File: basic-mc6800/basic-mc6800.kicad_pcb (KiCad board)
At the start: 2 copper layers, 100 x 45 mm, 21 parts, among them J1 Conn_01x39_Male, Q1 Q_NMOS_GSD, Q2 Q_NMOS_GSD, U1 74LS137, U2 MC6809, U3 IS61C256AL, U4 28C256, Y1 2-4Mhz

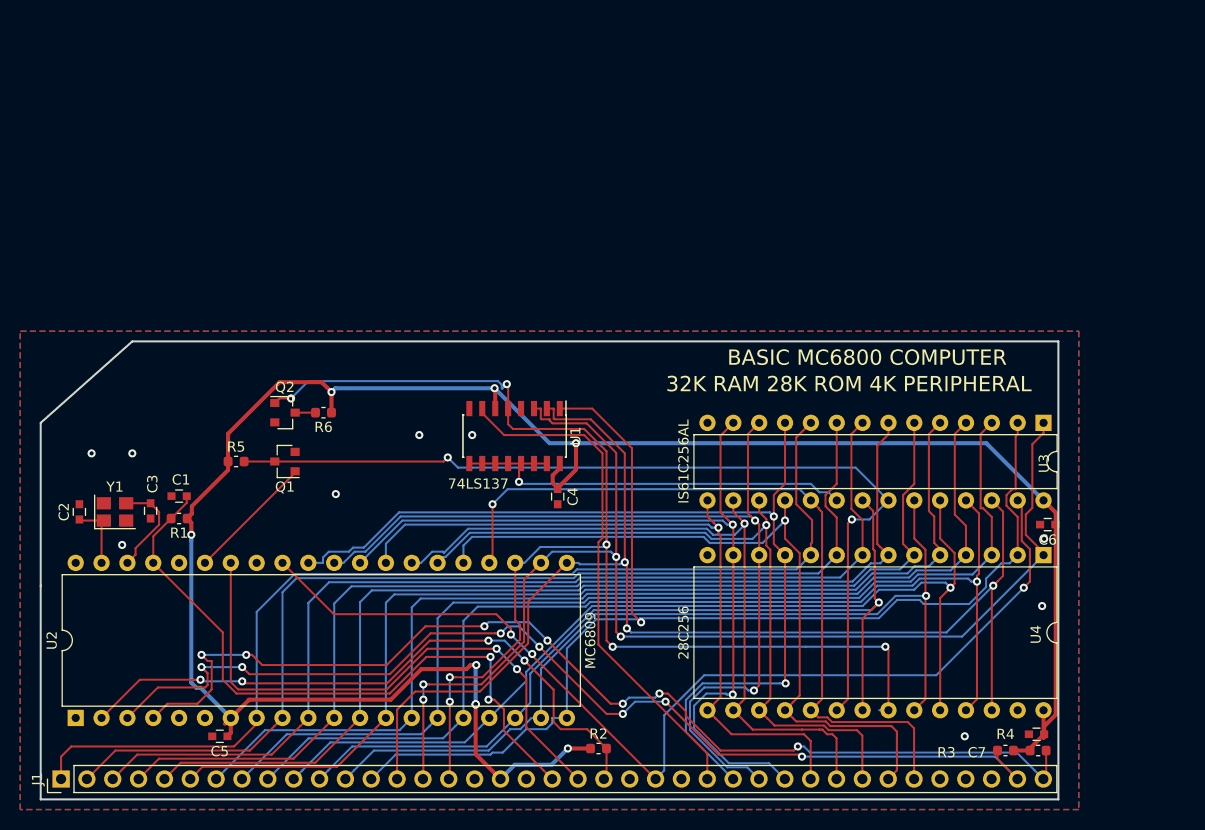
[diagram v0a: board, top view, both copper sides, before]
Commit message: swapped rom to top of memory and some fixes DRC done
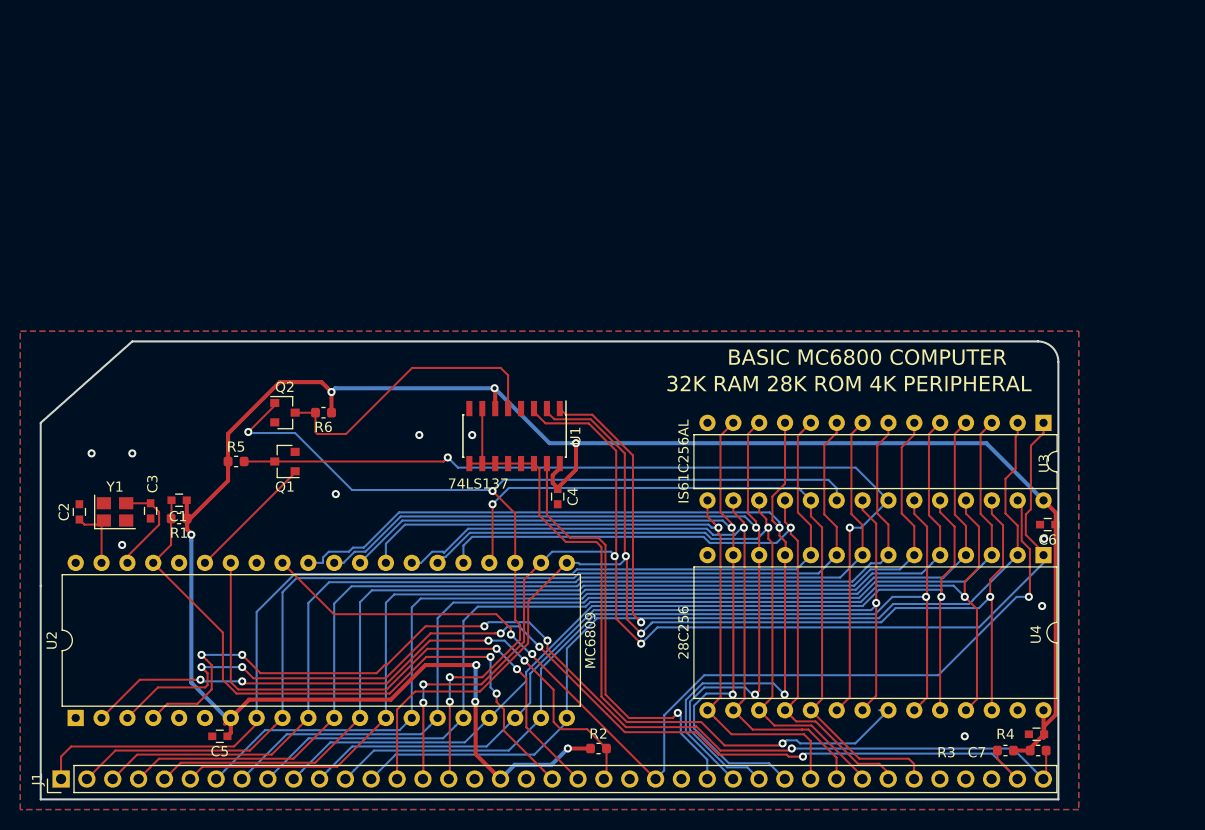
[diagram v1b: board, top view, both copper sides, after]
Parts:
- moved C1 0.40 mm to (111.6, 72.6)
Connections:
- C1 pad 1: /RESET -> +5V
- C1 pad 2: GND -> /RESET
- J1 pad 19: /M1 -> (no net)
- J1 pad 23: /MEM_REQ -> (no net)
- J1 pad 25: /RO -> (no net)
- J1 pad 35: /RX -> (no net)
- J1 pad 36: /TX -> (no net)
- J1 pad 37: /USR1 -> (no net)
- U1 pad 15: /ROM_CS -> /PER_CS
- U1 pad 5: /A15 -> /_A15
- U1 pad 7: /PER_CS -> /ROM_CS
- U2 pad 33: Net-(U2-Pad33) -> (no net)
- U2 pad 36: Net-(U2-Pad36) -> (no net)
- U2 pad 40: Net-(U2-Pad40) -> (no net)
- U2 pad 5: /BS -> (no net)
- U2 pad 6: /BA -> (no net)
- U3 pad 20: /ROM_CS -> /A15
- U4 pad 22: /A15 -> /ROM_CS
- U4 pad 27: Net-(U4-Pad27) -> (no net)
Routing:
- net /ROM_CS: track 41.5 -> 72.0 mm
- net /A15: track 128.6 -> 100.3 mm, vias 7 -> 4
- net /_A15: track 2.00 -> 29.2 mm
- net /PER_CS: track 50.5 -> 42.7 mm, vias 0 -> 1
- net /D6: track 73.5 -> 70.1 mm
- net +5V: track 213.2 -> 216.5 mm, vias 8 -> 7
- net /D0: track 95.0 -> 97.9 mm
- net /D5: track 71.3 -> 69.2 mm
- net /D7: track 75.7 -> 73.7 mm
- net /RESET: track 65.7 -> 64.1 mm
- net /D4: track 71.8 -> 70.4 mm
- net /A12: track 118.4 -> 117.2 mm
- net /D1: track 89.4 -> 90.4 mm
- net /R_W: track 102.4 -> 103.2 mm
- net Net-(C2-Pad1): track 6.69 -> 5.88 mm
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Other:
- outline, holes or cut-outs redrawn

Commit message: added bottom silk
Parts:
- added G***: LOGO, artandsilk:REARSILK, B.Cu at (148.0, 78.4)

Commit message: silks done tied mrdy high  gerder gened
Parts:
- moved G*** 0.36 mm to (148.3, 78.6)
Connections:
- U2 pad 36: (no net) -> +5V
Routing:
- net +5V: track 216.5 -> 219.7 mm
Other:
- board text added: "0x9000-0xFFFF ROM 0x8000-0x8FFF PERIPH 0x0000-0x7FFF RAM"
- board text added: "2MHz Power"
- board text added: "59 Instructions"
- board text added: "ALL DAT ROM!!!! NOM NOM"
- board text added: "MORE RAM THAN A FIELD OF SHEEP"
- board text added: "MPU POWER!!!"
- board text added: "by Rabid Inventor"

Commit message: tidied some traces and started io board v1 gerber here
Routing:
- net /INT3: track 106.3 -> 99.6 mm, vias 5 -> 2
- net +5V: track 219.7 -> 214.1 mm, vias 7 -> 5
- net /INT2: track 104.5 -> 99.8 mm, vias 5 -> 2
- net /INT1: track 62.4 -> 58.2 mm, vias 4 -> 0
- net /A13: track 123.9 -> 128.1 mm, vias 3 -> 5
- net /R_W: track 103.2 -> 107.2 mm, vias 3 -> 2
- net /A14: track 125.6 -> 128.7 mm
- net /E: track 55.9 -> 53.3 mm, vias 2 -> 1
- net /A12: track 117.2 -> 114.8 mm
- net /A11: track 89.0 -> 86.7 mm
- net /A10: track 85.4 -> 83.6 mm
- net /A15: track 100.3 -> 99.3 mm
- net /A9: track 94.4 -> 93.8 mm
- net /RESET: track 64.1 -> 64.4 mm, vias 2 -> 1

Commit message: started on version 1.1
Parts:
- removed C4: C_Small, Capacitors_SMD:C_0603
- removed G***: LOGO, artandsilk:REARSILK
- removed Q1, Q2: Q_NMOS_GSD, TO_SOT_Packages_SMD:SOT-23
- removed R5, R6: 100k, Resistor_SMD:R_0603_1608Metric
- added C8: C_Small, Capacitors_SMD:C_0603, F.Cu at (137.6, 64.2)
- added C9: C_Small, Capacitors_SMD:C_0603, F.Cu at (117.6, 63.2)
- added U5: 74LS14, Housings_SOIC:SOIC-14_3.9x8.7mm_Pitch1.27mm, F.Cu at (124.6, 65.2)
- U1: value 74LS137 -> 74LS32; footprint Housings_SOIC:SOIC-16_3.9x9.9mm_Pitch1.27mm -> Housings_SOIC:SOIC-14_3.9x8.7mm_Pitch1.27mm
- moved U1 0.38 mm to (144.8, 66.6), turned to 90 degrees
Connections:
- J1 pad 19: (no net) -> /M1
- J1 pad 23: (no net) -> /MEM_REQ
- J1 pad 25: (no net) -> /RO
- J1 pad 35: (no net) -> /RX
- J1 pad 36: (no net) -> /TX
- J1 pad 37: (no net) -> /USR1
- U1 pad 10: /ROM_CS -> /_A15
- U1 pad 12: /ROM_CS -> Net-(U1-Pad12)
- U1 pad 13: /ROM_CS -> /_A15
- U1 pad 14: /ROM_CS -> +5V
- U1 pad 3: /A14 -> Net-(U1-Pad3)
- U1 pad 4: GND -> Net-(U1-Pad3)
- U1 pad 5: /_A15 -> Net-(U1-Pad5)
- U1 pad 6: +5V -> /PER_CS
- U1 pad 7: /ROM_CS -> GND
- U1 pad 8: GND -> Net-(U1-Pad5)
- U1 pad 9: /ROM_CS -> /A14
- U2 pad 33: (no net) -> Net-(U2-Pad33)
- U2 pad 40: (no net) -> Net-(U2-Pad40)
- U2 pad 5: (no net) -> /BS
- U2 pad 6: (no net) -> /BA
- U4 pad 27: (no net) -> Net-(U4-Pad27)
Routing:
- net +5V: track 214.1 -> 0.00 mm, vias 5 -> 0
- net /A14: track 128.7 -> 0.00 mm, vias 4 -> 0
- net /A13: track 128.1 -> 0.00 mm, vias 5 -> 0
- net /R_W: track 107.2 -> 0.00 mm, vias 2 -> 0
- net /A0: track 104.6 -> 0.00 mm
- net /A1: track 104.0 -> 0.00 mm
- net /A4: track 103.5 -> 0.00 mm
- net /A5: track 103.3 -> 0.00 mm
- net /A2: track 103.3 -> 0.00 mm
- net /A3: track 103.3 -> 0.00 mm
- net /A6: track 103.1 -> 0.00 mm
- net /INT2: track 99.8 -> 0.00 mm, vias 2 -> 0
- net /INT3: track 99.6 -> 0.00 mm, vias 2 -> 0
- net /A15: track 99.3 -> 0.00 mm, vias 4 -> 0
- net /D0: track 97.6 -> 0.00 mm, vias 2 -> 0
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
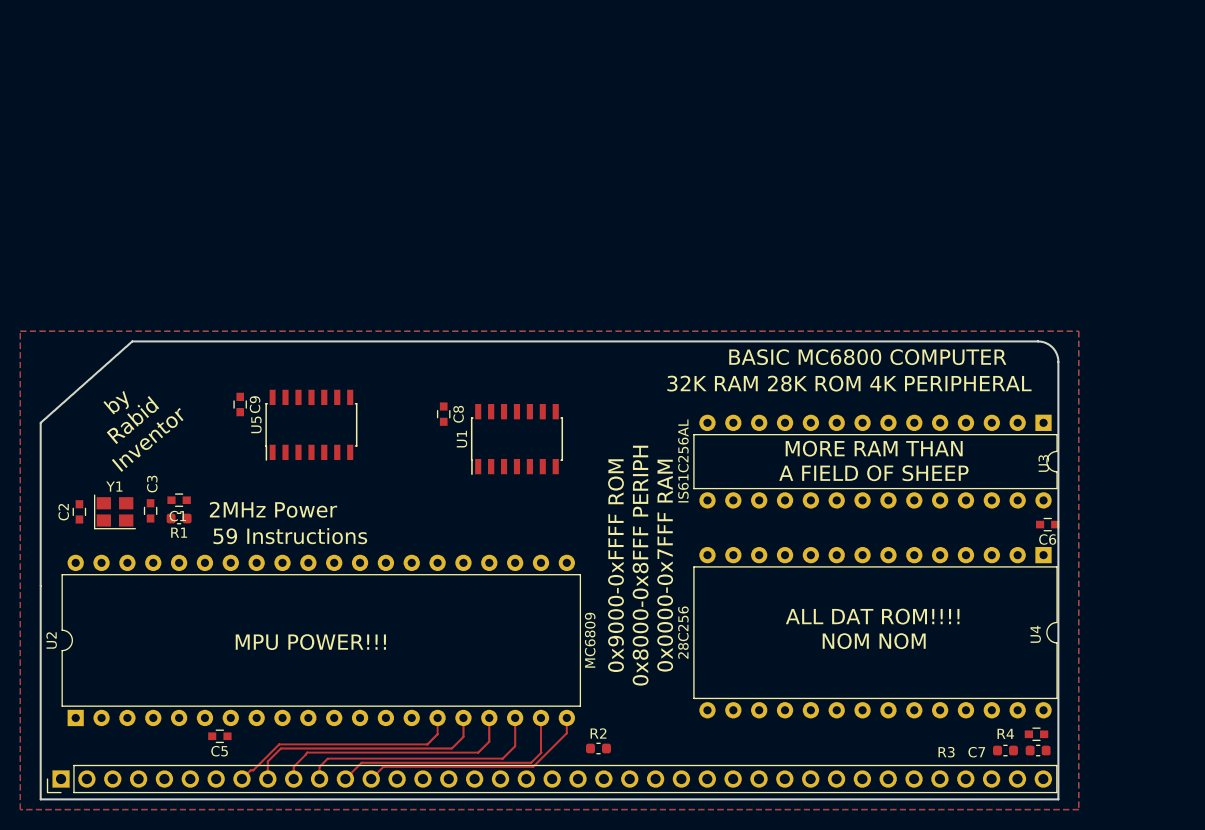
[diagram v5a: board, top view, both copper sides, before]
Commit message: changed part vaules to match what is available
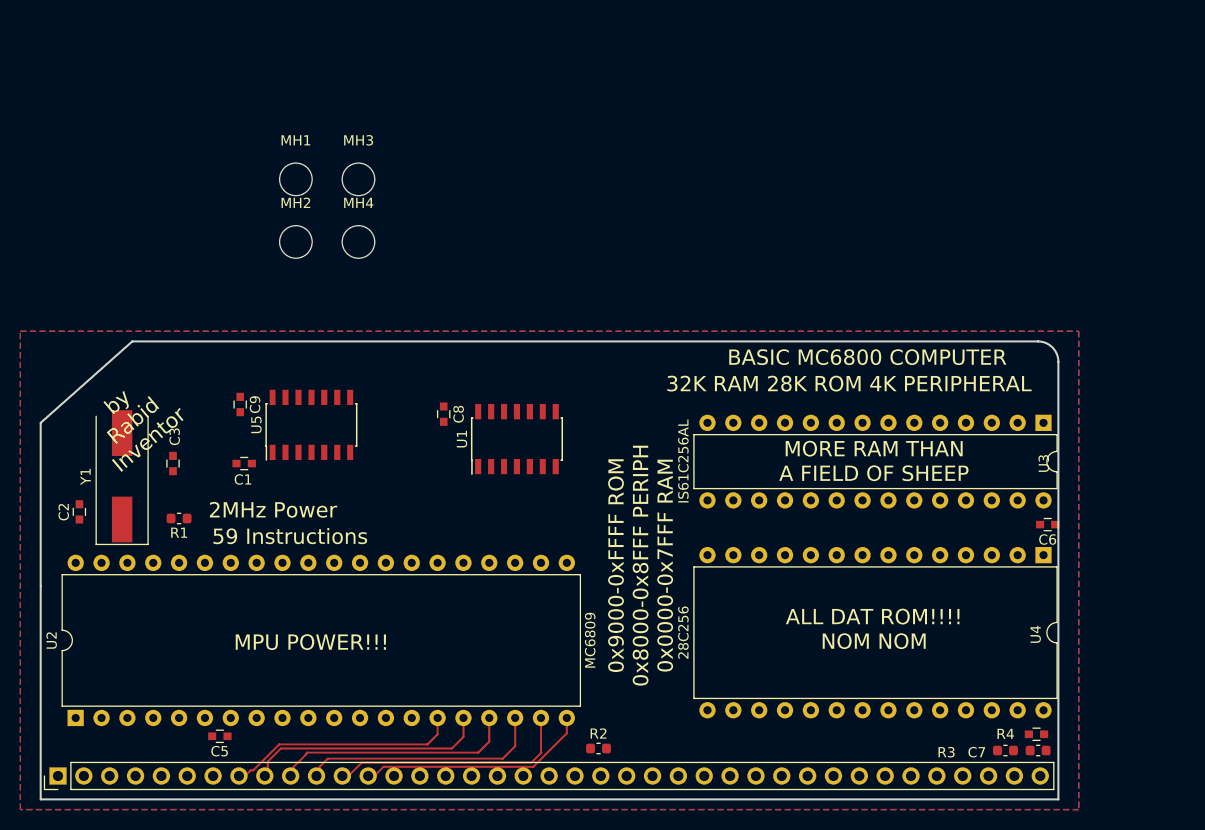
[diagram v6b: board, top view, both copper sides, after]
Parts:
- added MH1: MountingHole, Mounting_Holes:MountingHole_3.2mm_M3_DIN965, F.Cu at (123.1, 41.1)
- added MH2: MountingHole, Mounting_Holes:MountingHole_3.2mm_M3_DIN965, F.Cu at (123.1, 47.2)
- added MH3: MountingHole, Mounting_Holes:MountingHole_3.2mm_M3_DIN965, F.Cu at (129.2, 41.1)
- added MH4: MountingHole, Mounting_Holes:MountingHole_3.2mm_M3_DIN965, F.Cu at (129.2, 47.2)
- U1: value 74LS32 -> 74LV32
- U5: value 74LS14 -> 74LV14
- Y1: value 2-4Mhz -> ABLS-4.000MHZ-20-B-3-H-T; footprint Crystal:Crystal_SMD_3225-4Pin_3.2x2.5mm -> Crystal:Crystal_SMD_HC49-SD
- moved C1 7.34 mm to (118.0, 69.0)
- moved C3 5.14 mm to (111.0, 69.0)
- moved Y1 3.57 mm to (106.0, 70.2), turned to 90 degrees
- moved J1 0.42 mm to (99.7, 99.7)
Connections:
- Y1 pad 2: GND -> Net-(C3-Pad1)

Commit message: backup checkin
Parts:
- added J2: Conn_01x04_Male, Connector_PinSocket_2.54mm:PinSocket_1x04_P2.54mm_Vertical, F.Cu at (128.0, 59.0)
- added JP1: Jumper_2_Open, Jumper:SolderJumper-2_P1.3mm_Bridged_RoundedPad1.0x1.5mm, F.Cu at (193.7, 87.0)
- added JP2: Jumper_2_Open, Jumper:SolderJumper-2_P1.3mm_Bridged_RoundedPad1.0x1.5mm, B.Cu at (207.7, 88.3)
- added JP3: Jumper_2_Open, Jumper:SolderJumper-2_P1.3mm_Bridged_RoundedPad1.0x1.5mm, B.Cu at (204.4, 88.3)
- added R5: R_Small, Resistor_SMD:R_0603_1608Metric, F.Cu at (114.6, 75.6)
- added R6: R_Small, Resistor_SMD:R_0603_1608Metric, F.Cu at (100.8, 76.2)
- added R7: R_Small, Resistor_SMD:R_0603_1608Metric, F.Cu at (114.6, 74.1)
- added R8: R_Small, Resistor_SMD:R_0603_1608Metric, F.Cu at (193.6, 83.2)
- moved MH3 68.4 mm to (195.0, 60.0)
- moved MH1 61.2 mm to (157.0, 92.0)
- moved MH2 36.3 mm to (157.0, 60.0)
- moved MH4 20.7 mm to (113.0, 60.0)
- moved C1 8.52 mm to (111.1, 74.0)
- moved C8 4.32 mm to (139.5, 60.2), turned to 180 degrees
- moved C3 2.30 mm to (110.5, 66.8)
- moved U1 1.79 mm to (144.0, 65.0)
- moved R1 1.21 mm to (111.1, 75.5)
- moved C6 0.70 mm to (196.2, 75.0)
- moved C9 0.45 mm to (118.0, 63.0), turned to 180 degrees
- moved C5 0.39 mm to (115.9, 96.0)
- moved C7 0.22 mm to (196.1, 95.5)
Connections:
- J1 pad 25: /RO -> /READ_OUT
- J1 pad 38: /INT2 -> Net-(J1-Pad38)
- J1 pad 39: /INT3 -> Net-(J1-Pad39)
- U2 pad 33: Net-(U2-Pad33) -> /_DMA
- U2 pad 36: +5V -> /MRDY
- U2 pad 40: Net-(U2-Pad40) -> /_HALT
- U5 pad 1: /QLATCH -> /R_W
- U5 pad 10: (no net) -> Net-(J2-Pad1)
- U5 pad 11: (no net) -> Net-(J2-Pad2)
- U5 pad 12: (no net) -> Net-(J2-Pad3)
- U5 pad 13: (no net) -> Net-(J2-Pad4)
- U5 pad 2: /_QLATCH -> /READ_OUT
- U5 pad 3: /A15 -> /QLATCH
- U5 pad 4: /_A15 -> /_QLATCH
- U5 pad 5: /PER_CS -> /A15
- U5 pad 6: Net-(U1-Pad12) -> /_A15
- U5 pad 8: (no net) -> Net-(U1-Pad12)
- U5 pad 9: (no net) -> /PER_CS
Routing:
- net +5V: track 0.00 -> 200.2 mm, vias 0 -> 7
- net /A6: track 0.00 -> 103.9 mm, vias 0 -> 1
- net /A5: track 0.00 -> 103.0 mm, vias 0 -> 1
- net /A0: track 0.00 -> 102.8 mm, vias 0 -> 1
- net /A3: track 0.00 -> 102.5 mm, vias 0 -> 1
- net /A2: track 0.00 -> 102.1 mm, vias 0 -> 1
- net /A4: track 0.00 -> 102.0 mm, vias 0 -> 1
- net /A1: track 0.00 -> 101.8 mm, vias 0 -> 1
- net /A13: track 0.00 -> 100.8 mm, vias 0 -> 2
- net /A14: track 0.00 -> 99.4 mm, vias 0 -> 2
- net /D0: track 0.00 -> 99.2 mm, vias 0 -> 3
- net /D1: track 0.00 -> 90.3 mm, vias 0 -> 3
- net /D2: track 0.00 -> 83.3 mm, vias 0 -> 3
- net /A7: track 22.6 -> 102.6 mm, vias 0 -> 1
- net /A8: track 23.8 -> 98.4 mm, vias 0 -> 1
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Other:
- board text added: "1MHz Power"
- board text removed: "2MHz Power"

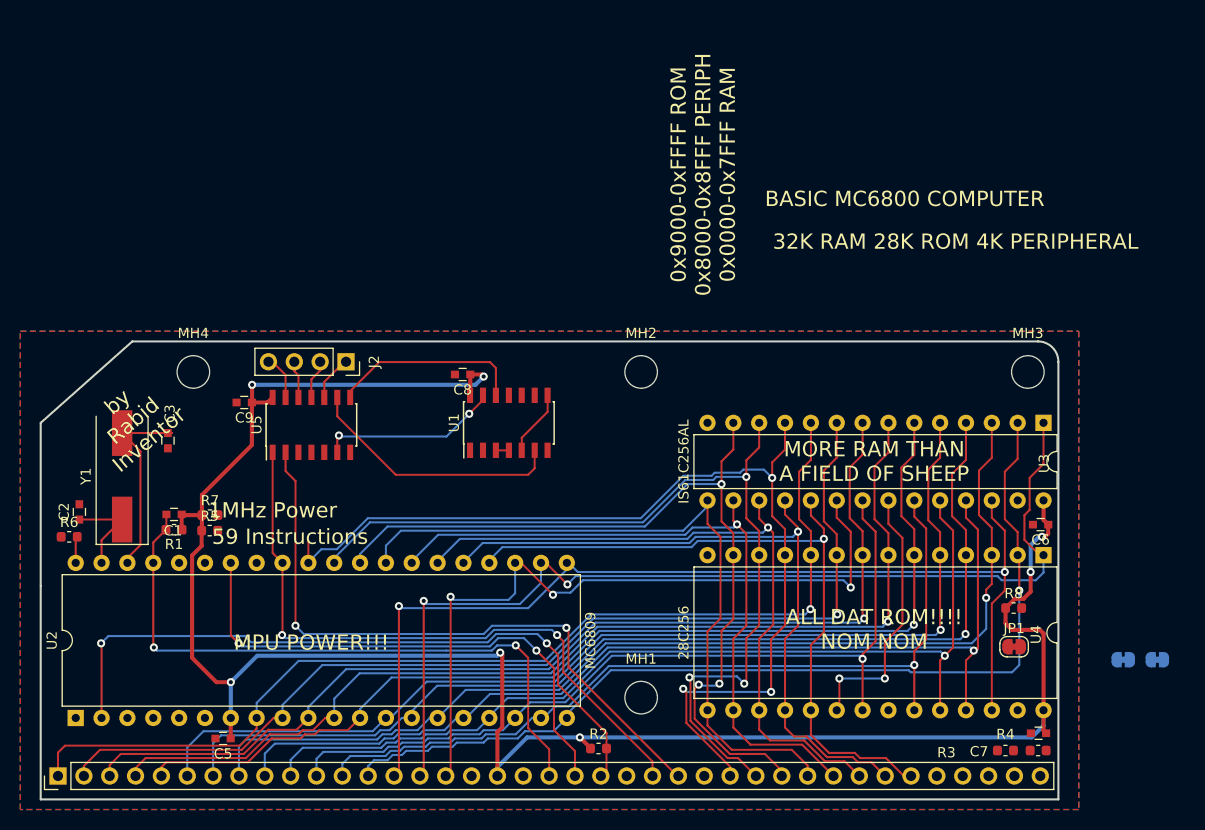
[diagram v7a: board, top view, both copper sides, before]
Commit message: COMPLETE V1B BASICMC6900 started battery backed 128K banked ram
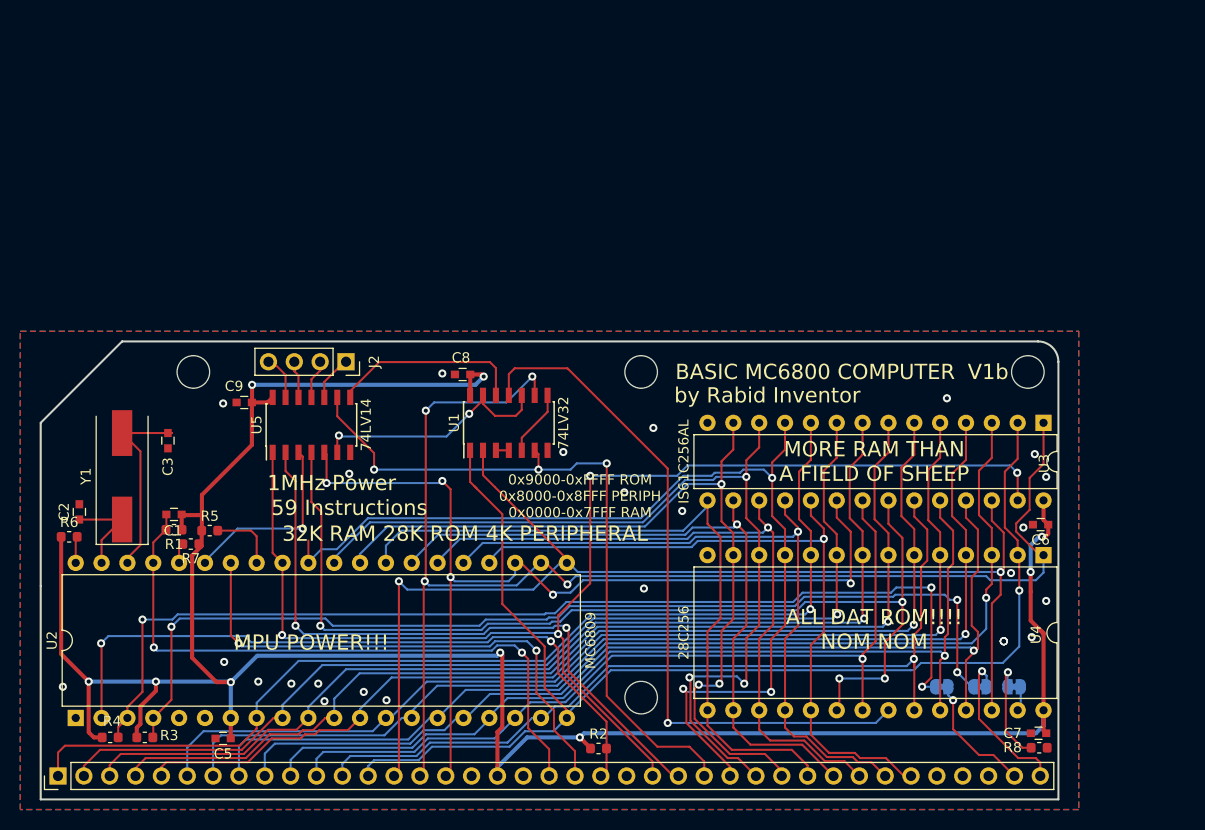
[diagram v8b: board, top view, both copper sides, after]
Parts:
- added G***: LOGO, artandsilk:REARSILK, B.Cu at (147.8, 78.5)
- JP1: moved to B.Cu
- moved R3 88.0 mm to (104.8, 95.9), turned to 0 degrees
- moved R4 87.8 mm to (108.2, 95.9)
- moved JP2 21.4 mm to (186.5, 90.9)
- moved JP3 14.3 mm to (190.3, 90.9)
- moved R8 14.0 mm to (196.1, 96.9), turned to 180 degrees
- moved JP1 3.93 mm to (193.7, 90.9)
- moved R7 3.41 mm to (112.8, 76.9), turned to 180 degrees
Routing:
- net /INT2: track 0.00 -> 102.8 mm, vias 0 -> 3
- net /INT3: track 0.00 -> 100.1 mm, vias 0 -> 3
- net /_QLATCH: track 26.5 -> 102.5 mm, vias 2 -> 4
- net /ROM_CS: track 0.00 -> 69.2 mm, vias 0 -> 1
- net /R_W: track 63.8 -> 125.9 mm, vias 2 -> 4
- net /PER_CS: track 25.7 -> 70.3 mm, vias 0 -> 3
- net +5V: track 200.2 -> 238.6 mm, vias 7 -> 9
- net /A14: track 99.4 -> 130.7 mm, vias 2 -> 4
- net /A12: track 94.4 -> 123.6 mm
- net /A15: track 71.8 -> 95.7 mm, vias 3 -> 5
- net /QLATCH: track 0.00 -> 18.8 mm, vias 0 -> 1
- net Net-(J1-Pad39): track 0.00 -> 15.6 mm, vias 0 -> 1
- net /A13: track 100.8 -> 116.3 mm
- net Net-(J1-Pad38): track 0.00 -> 12.3 mm, vias 0 -> 1
- net Net-(JP1-Pad1): track 0.00 -> 10.5 mm, vias 0 -> 1
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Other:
- outline, holes or cut-outs redrawn
- board text added: "CUT TO DISABLE"
- board text added: "FIRQ"
- board text added: "IRQ"
- board text added: "ROM_WP"
- board text added: "V1b"
